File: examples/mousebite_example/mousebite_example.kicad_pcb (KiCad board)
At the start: 4 copper layers, 99.1 x 34.3 mm, 1 part

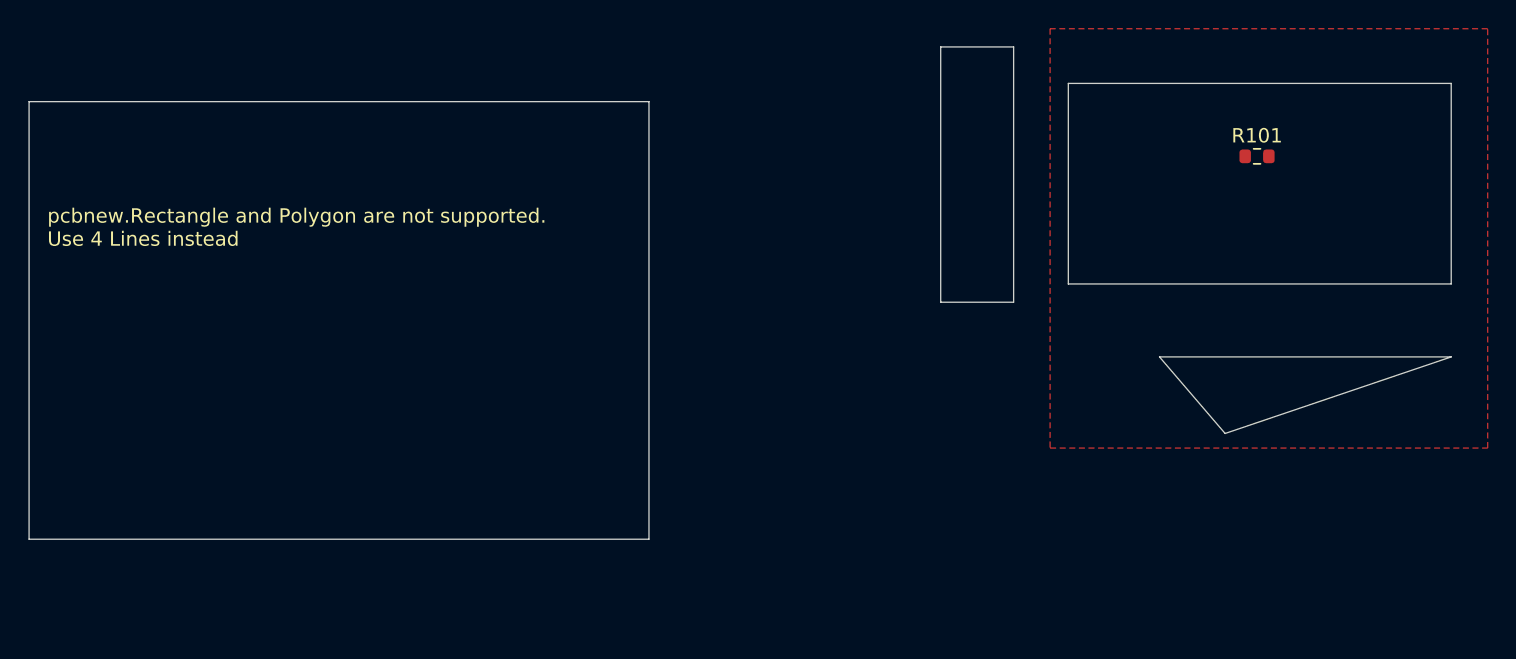
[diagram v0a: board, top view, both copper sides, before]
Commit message: Mousebite better
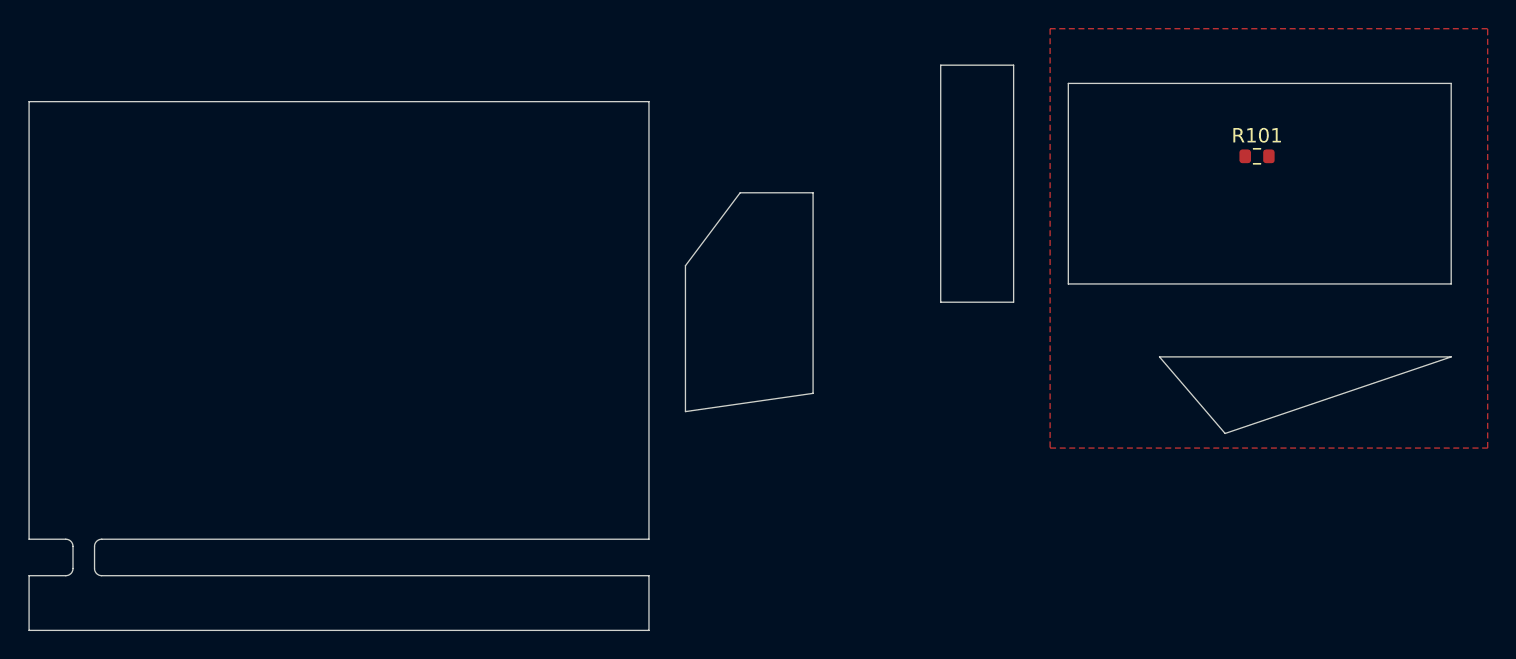
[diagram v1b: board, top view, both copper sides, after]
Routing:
- net (no net): vias 0 -> 10
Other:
- board size 99.1 x 34.3 mm -> 99.1 x 39.4 mm
- board text added: "Make these look like that one"
- board text removed: "pcbnew.Rectangle and Polygon are not supported. Use 4 Lines instead"
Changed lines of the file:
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@@
   (gr_line (start 173.736 80.518) (end 173.736 89.408)
+    (stroke (width 0.1) (type default)) (layer "Eco1.User"))
+  (gr_line (start 120.396 86.868) (end 128.016 86.868)
+    (stroke (width 0.1) (type default)) (layer "Eco1.User"))
+  (gr_line (start 133.096 80.518) (end 144.526 80.518)
     (stroke (width 0.1) (type default)) (layer "Eco1.User"))
   (gr_line (start 164.846 80.518) (end 164.846 90.678)
@@
   (gr_line (start 147.066 72.898) (end 153.416 72.898)
     (stroke (width 0.1) (type default)) (layer "Eco1.User"))
+  (gr_line (start 106.426 99.568) (end 106.426 104.648)
+    (stroke (width 0.1) (type default)) (layer "Eco2.User"))
+  (gr_line (start 98.806 99.568) (end 98.806 104.648)
+    (stroke (width 0.1) (type default)) (layer "Eco2.User"))
+  (gr_line (start 91.186 99.568) (end 91.186 104.648)
+    (stroke (width 0.1) (type default)) (layer "Eco2.User"))
+  (gr_line (start 114.046 99.568) (end 114.046 104.648)
+    (stroke (width 0.1) (type default)) (layer "Eco2.User"))
+  (gr_rect (start 143.256 67.818) (end 148.336 84.328)
+    (stroke (width 0.05) (type default)) (fill none) (layer "Edge.Cuts"))
   (gr_line (start 158.496 88.138) (end 163.068 93.472)
+    (stroke (width 0.05) (type default)) (layer "Edge.Cuts"))
+  (gr_line (start 82.816 101.338) (end 82.816 102.878)
+    (stroke (width 0.05) (type default)) (layer "Edge.Cuts"))
+  (gr_arc (start 84.316 101.338) (mid 84.462447 100.984447) (end 84.816 100.838)
+    (stroke (width 0.05) (type default)) (layer "Edge.Cuts"))
+  (gr_line (start 79.756 100.838) (end 79.756 70.358)
     (stroke (width 0.05) (type default)) (layer "Edge.Cuts"))
   (gr_line (start 178.816 88.138) (end 163.068 93.472)
@@
   (gr_line (start 152.146 83.058) (end 178.816 83.058)
     (stroke (width 0.05) (type default)) (layer "Edge.Cuts"))
-  (gr_line (start 143.256 84.328) (end 143.256 66.548)
+  (gr_line (start 122.936 107.188) (end 79.756 107.188)
+    (stroke (width 0.05) (type default)) (layer "Edge.Cuts"))
+  (gr_arc (start 82.816 102.878) (mid 82.669553 103.231553) (end 82.316 103.378)
     (stroke (width 0.05) (type default)) (layer "Edge.Cuts"))
   (gr_line (start 178.816 69.088) (end 178.816 83.058)
     (stroke (width 0.05) (type default)) (layer "Edge.Cuts"))
+  (gr_arc (start 84.816 103.378) (mid 84.462447 103.231553) (end 84.316 102.878)
+    (stroke (width 0.05) (type default)) (layer "Edge.Cuts"))
+  (gr_line (start 84.816 103.378) (end 122.936 103.378)
+    (stroke (width 0.05) (type default)) (layer "Edge.Cuts"))
   (gr_line (start 152.146 69.088) (end 178.816 69.088)
     (stroke (width 0.05) (type default)) (layer "Edge.Cuts"))
-  (gr_line (start 143.256 66.548) (end 148.336 66.548)
+  (gr_line (start 84.316 101.338) (end 84.316 102.878)
     (stroke (width 0.05) (type default)) (layer "Edge.Cuts"))
-  (gr_line (start 148.336 84.328) (end 143.256 84.328)
+  (gr_line (start 122.936 103.378) (end 122.936 107.188)
     (stroke (width 0.05) (type default)) (layer "Edge.Cuts"))
-  (gr_rect (start 79.756 70.358) (end 122.936 100.838)
-    (stroke (width 0.05) (type default)) (fill none) (layer "Edge.Cuts"))
+  (gr_line (start 82.316 100.838) (end 79.756 100.838)
+    (stroke (width 0.05) (type default)) (layer "Edge.Cuts"))
+  (gr_line (start 79.756 107.188) (end 79.756 103.378)
+    (stroke (width 0.05) (type default)) (layer "Edge.Cuts"))
+  (gr_arc (start 82.316 100.838) (mid 82.669553 100.984447) (end 82.816 101.338)
+    (stroke (width 0.05) (type default)) (layer "Edge.Cuts"))
   (gr_line (start 158.496 88.138) (end 178.816 88.138)
+    (stroke (width 0.05) (type default)) (layer "Edge.Cuts"))
+  (gr_poly
+    (pts
+      (xy 125.476 81.788)
+      (xy 125.476 91.948)
+      (xy 134.366 90.678)
+      (xy 134.366 76.708)
+      (xy 129.286 76.708)
+    )
+    (stroke (width 0.05) (type solid)) (fill none) (layer "Edge.Cuts"))
+  (gr_line (start 79.756 70.358) (end 122.936 70.358)
+    (stroke (width 0.05) (type default)) (layer "Edge.Cuts"))
+  (gr_line (start 122.936 70.358) (end 122.936 100.838)
+    (stroke (width 0.05) (type default)) (layer "Edge.Cuts"))
+  (gr_line (start 84.816 100.838) (end 122.936 100.838)
     (stroke (width 0.05) (type default)) (layer "Edge.Cuts"))
   (gr_line (start 152.146 83.058) (end 152.146 69.088)
     (stroke (width 0.05) (type default)) (layer "Edge.Cuts"))
-  (gr_line (start 148.336 66.548) (end 148.336 84.328)
+  (gr_line (start 82.316 103.378) (end 79.756 103.378)
     (stroke (width 0.05) (type default)) (layer "Edge.Cuts"))
-  (gr_text "pcbnew.Rectangle and Polygon are not supported.\nUse 4 Lines instead" (at 81.026 80.518) (layer "F.SilkS")
-    (effects (font (size 1 1) (thickness 0.1)) (justify left bottom))
+  (gr_text "Make these look like that one" (at 91.186 106.553) (layer "Eco2.User")
+    (effects (font (size 1 1) (thickness 0.15)) (justify left bottom))
   )
+  (via (at 83.566 103.478) (size 0.1) (drill 0.4) (layers "F.Cu" "B.Cu") (net 0))
+  (via (at 82.966 100.738) (size 0.1) (drill 0.4) (layers "F.Cu" "B.Cu") (net 0))
+  (via (at 83.566 100.738) (size 0.1) (drill 0.4) (layers "F.Cu" "B.Cu") (net 0))
+  (via (at 84.766 100.738) (size 0.1) (drill 0.4) (layers "F.Cu" "B.Cu") (net 0))
+  (via (at 84.166 100.738) (size 0.1) (drill 0.4) (layers "F.Cu" "B.Cu") (net 0))
+  (via (at 82.966 103.478) (size 0.1) (drill 0.4) (layers "F.Cu" "B.Cu") (net 0))
+  (via (at 82.366 100.738) (size 0.1) (drill 0.4) (layers "F.Cu" "B.Cu") (net 0))
+  (via (at 84.766 103.478) (size 0.1) (drill 0.4) (layers "F.Cu" "B.Cu") (net 0))
+  (via (at 82.366 103.478) (size 0.1) (drill 0.4) (layers "F.Cu" "B.Cu") (net 0))
+  (via (at 84.166 103.478) (size 0.1) (drill 0.4) (layers "F.Cu" "B.Cu") (net 0))
   (zone (net 2) (net_name "GND") (layer "F.Cu") (hatch edge 0.5)
     (connect_pads thru_hole_only (clearance 0.5))
